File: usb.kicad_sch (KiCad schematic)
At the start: 125 parts, among them J3 USB4105-GF-A, J4 WE_632723300011_alt_symbol, Q1 PJE138K, U10 TUSB1046-DCI, U11 TPD4E05U06QDQARQ1, U12 AP22615, U13 TPD4E05U06QDQARQ1, U14 TPD4E05U06QDQARQ1, U15 TPD4E05U06QDQARQ1, U16 TPD4E05U06QDQARQ1, U5 FT230XQ-R, U6 TPS65988, U7 W25Q80DVUXIE_TR, U8 NCP730BMT330TBG, U9 AP22615

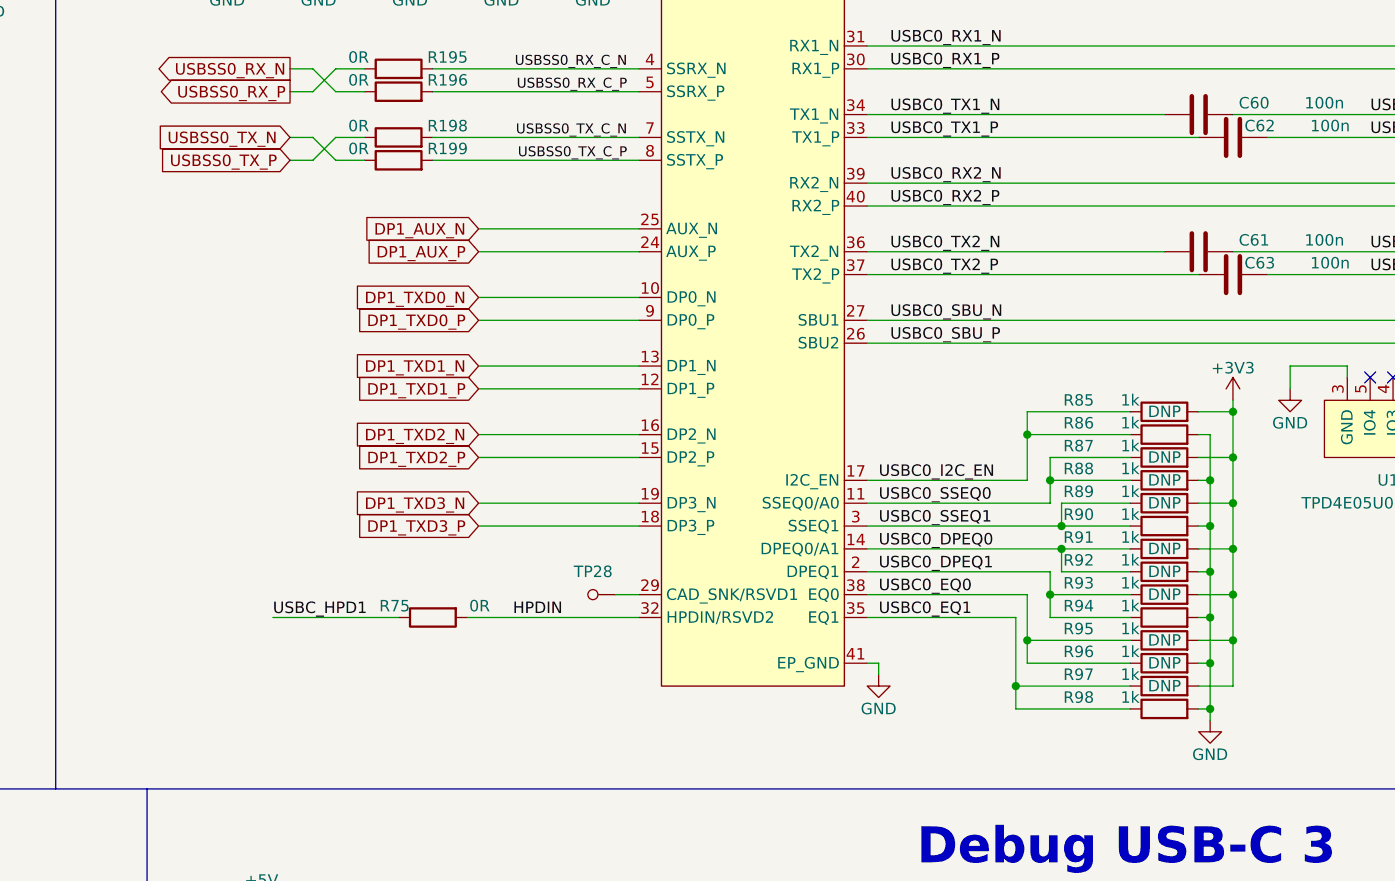
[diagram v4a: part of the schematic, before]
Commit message: Add missing DP AUX pullup/down resistors
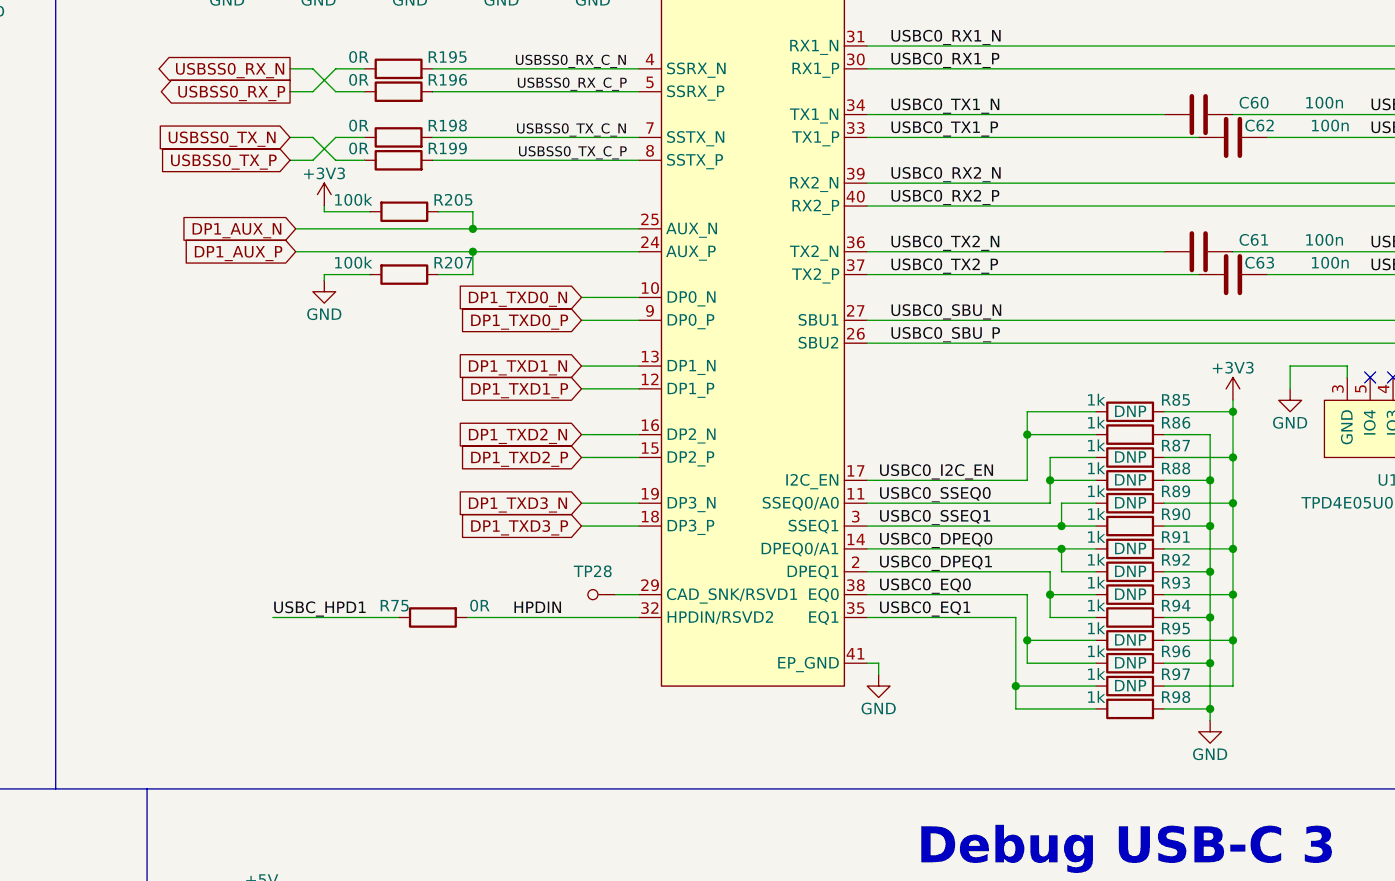
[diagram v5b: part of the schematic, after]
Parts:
- added R205, R207: R_100k_0402, jetson-orin-baseboard-footprints:0402-res, symbol jetson-orin-baseboard:R_100k_0402
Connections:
- net +3V3: now also R205.2
- net DP1_AUX_N: now also R205.1
- net DP1_AUX_P: now also R207.1
- net GND: now also R207.2
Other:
- moved on the sheet: R85, R86, R87, R88, R89, R90, R91, R92, R93, R94, R95, R96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

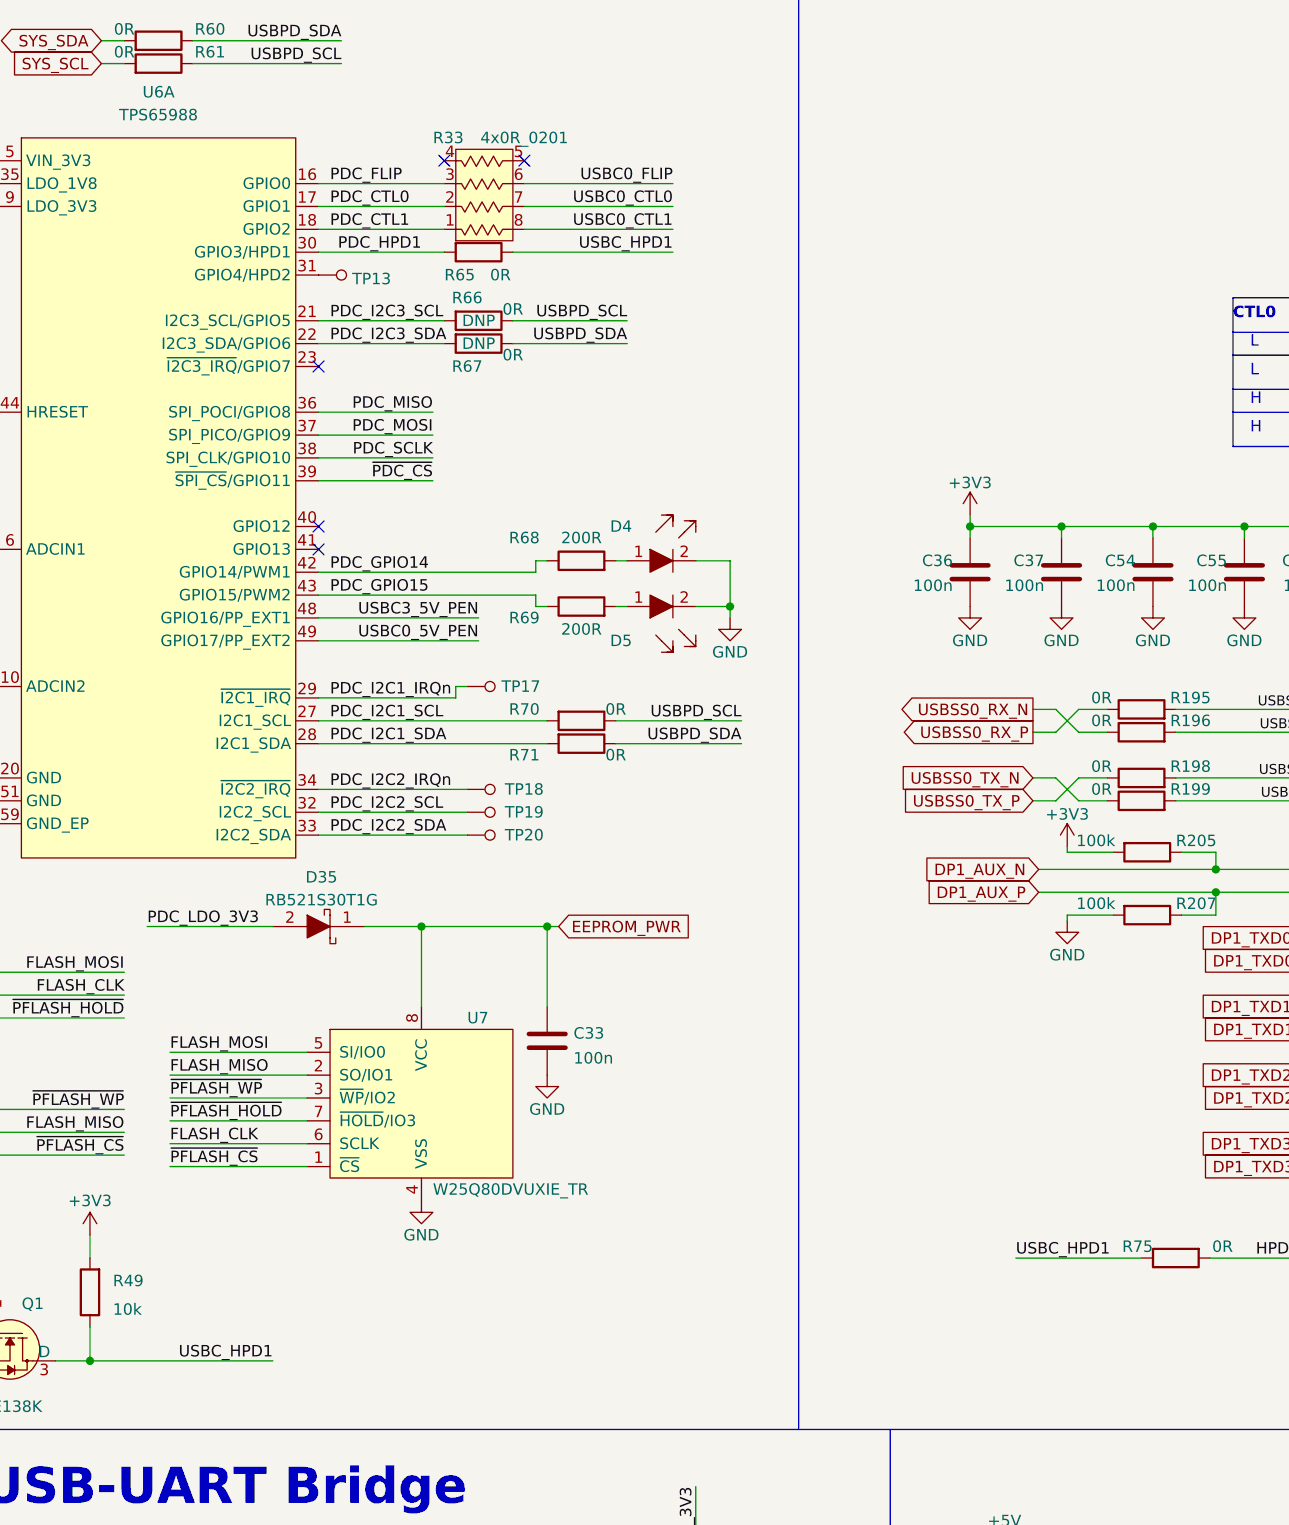
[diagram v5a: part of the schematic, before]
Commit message: Connect USB-C HPD to correct pin
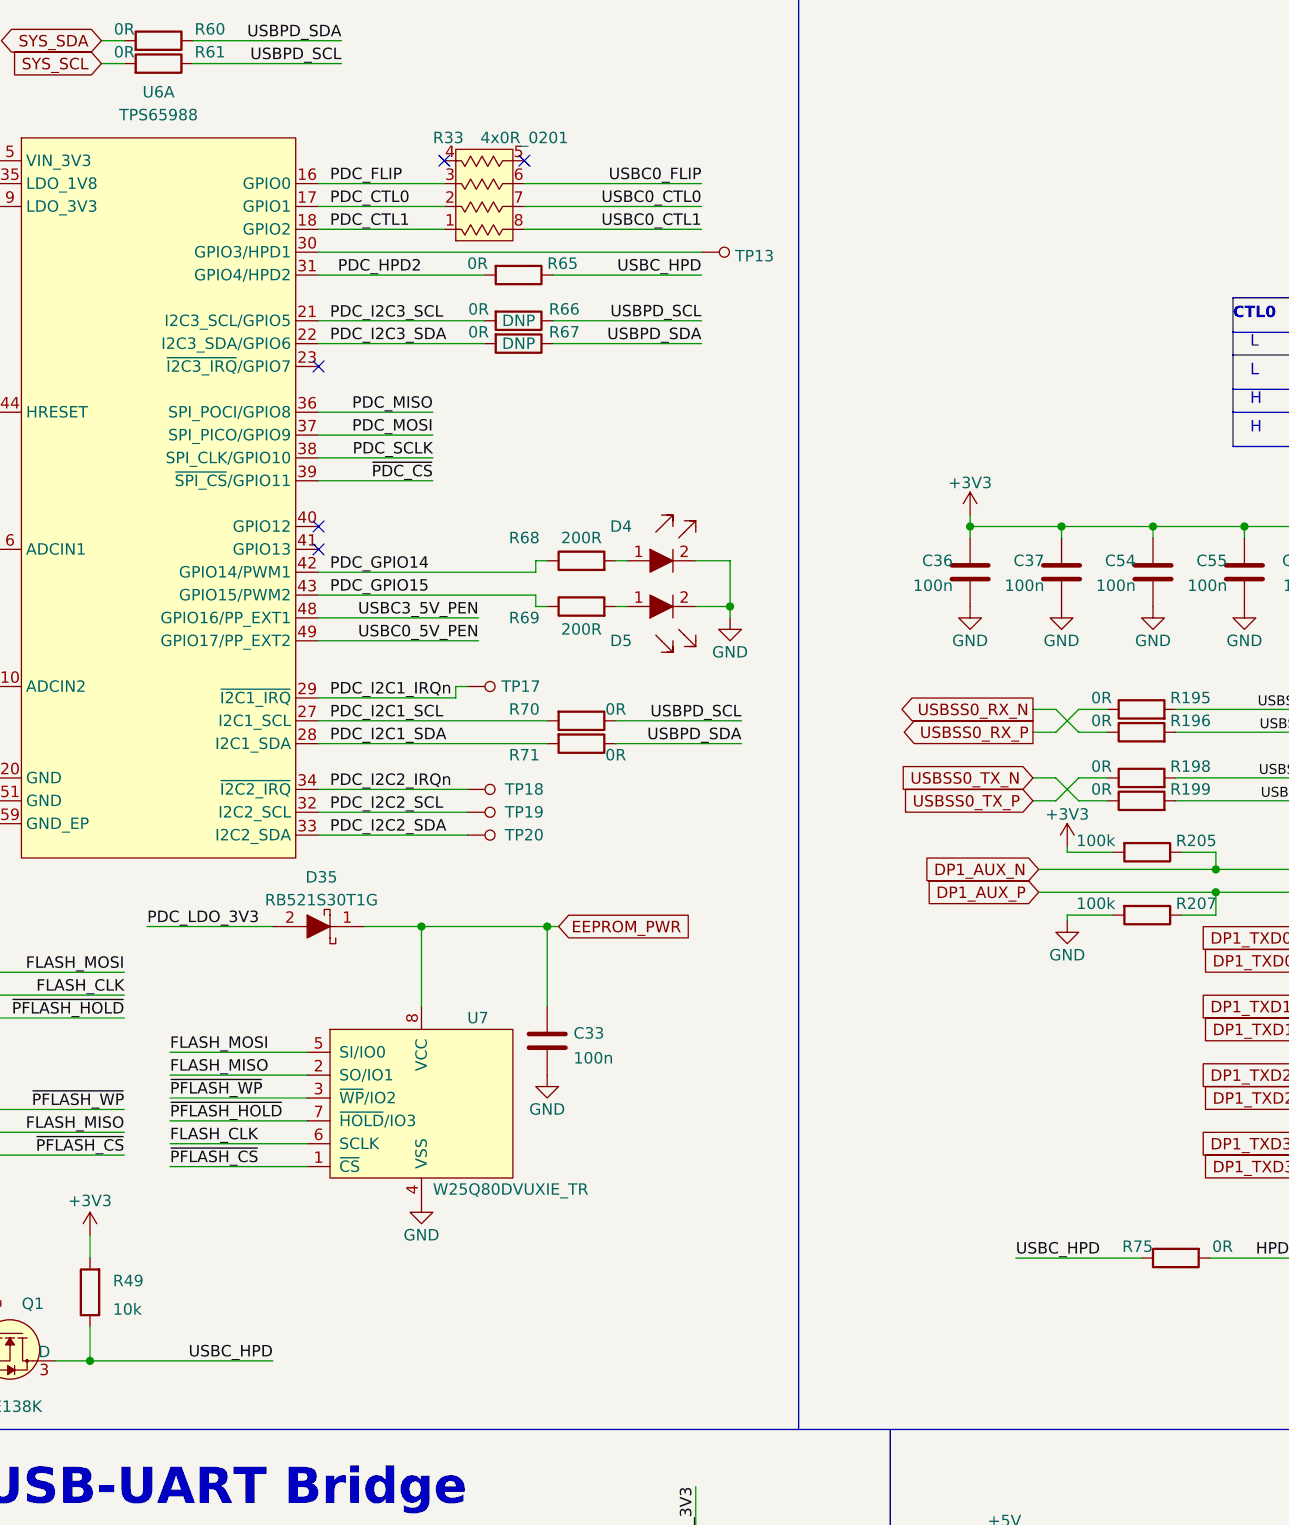
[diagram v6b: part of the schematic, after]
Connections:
- net PDC_I2C3_SCL: no longer R66.2, U6.21 (I2C3_SCL/GPIO5)
- net at TP13.1: now also U6.30 (GPIO3/HPD1); no longer U6.31 (GPIO4/HPD2)
- net PDC_HPD1 renamed PDC_HPD2
- net PDC_HPD2: now also U6.31 (GPIO4/HPD2); no longer U6.30 (GPIO3/HPD1)
- net USBC_HPD1 renamed USBC_HPD
- new net: R66.2, U6.21 (I2C3_SCL/GPIO5)
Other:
- moved on the sheet: R65, R66, R67, TP13

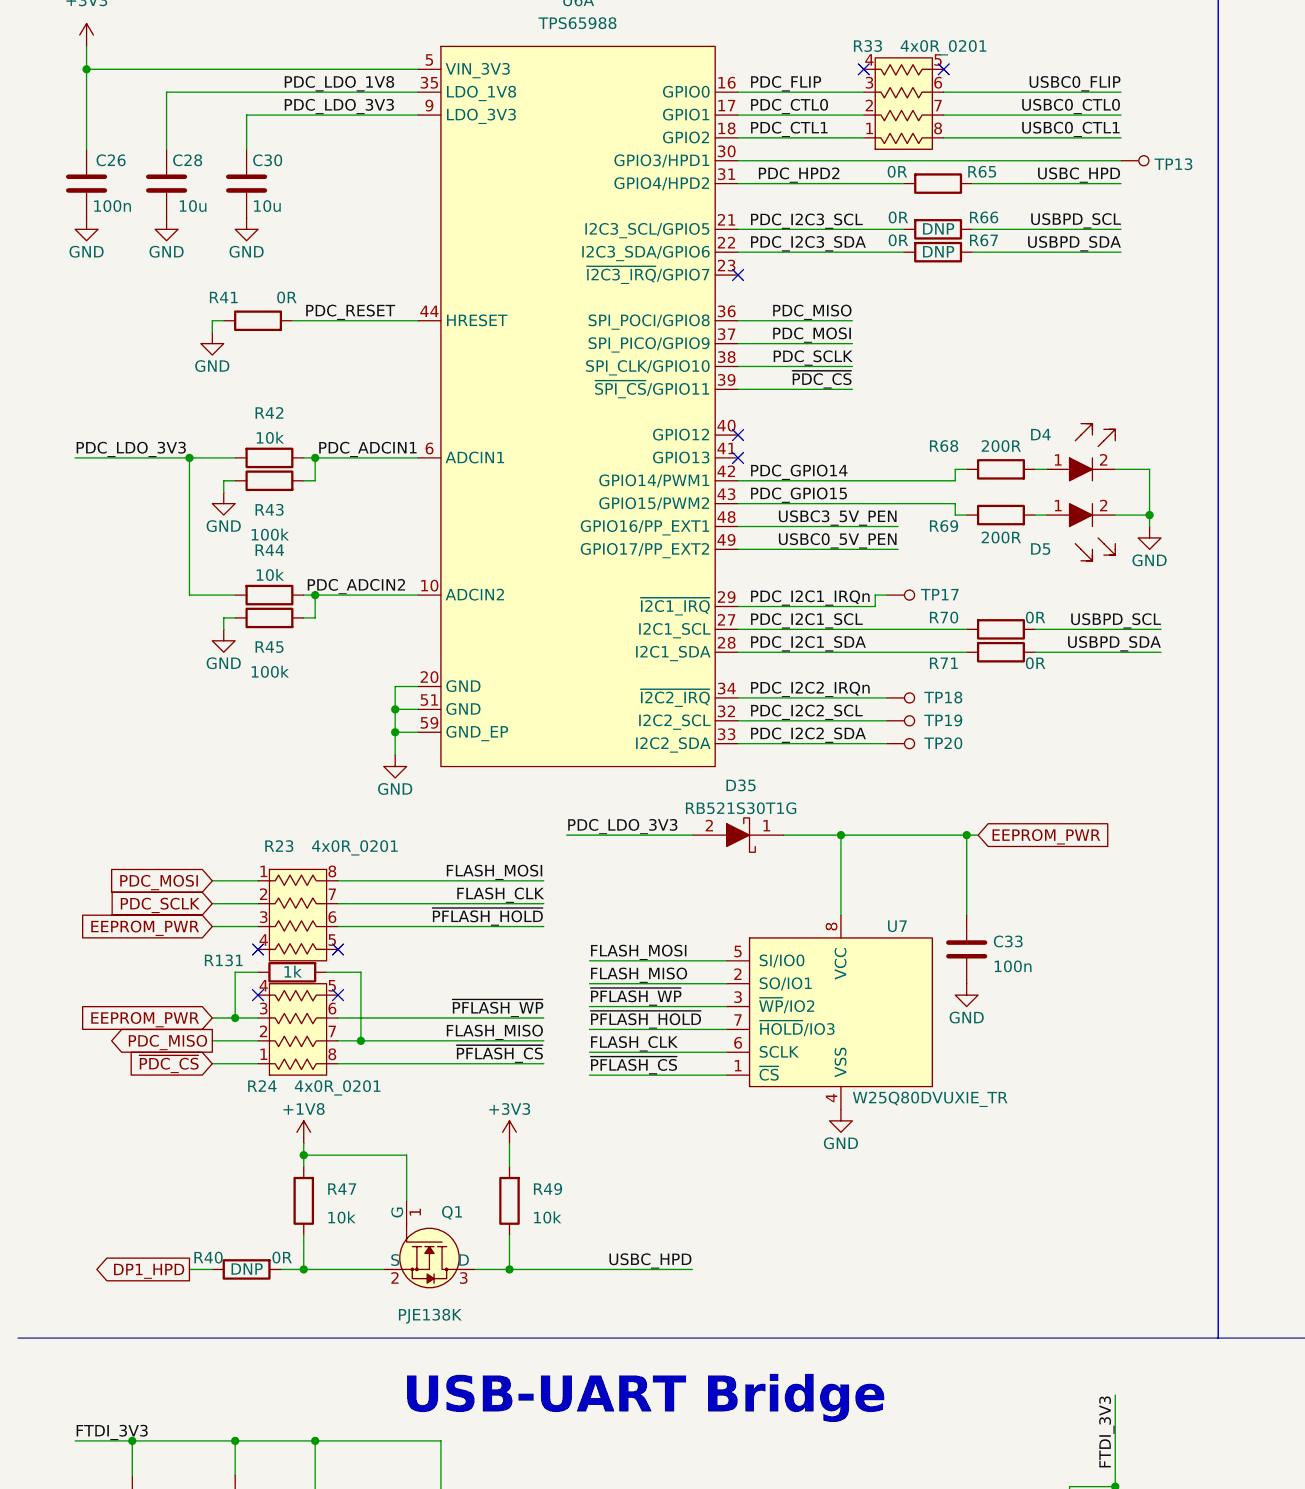
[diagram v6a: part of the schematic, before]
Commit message: Use DP switch in place of selection via mounting option
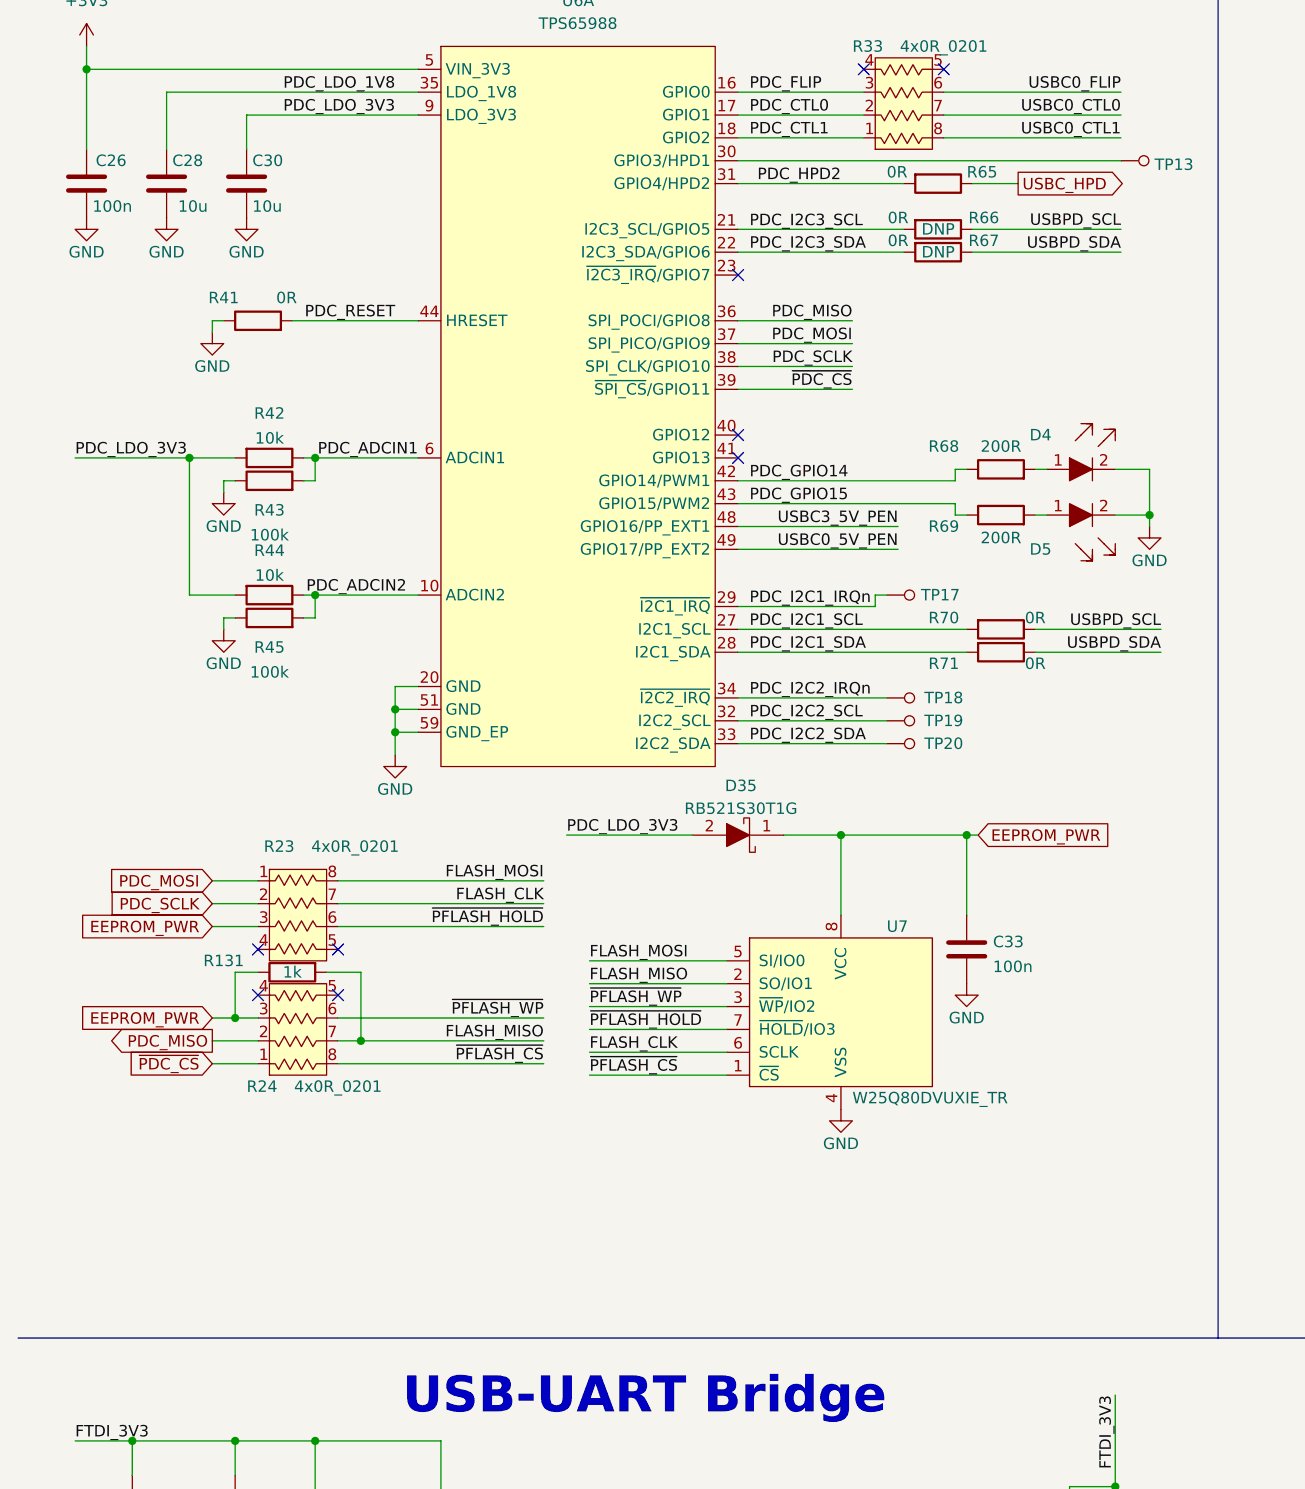
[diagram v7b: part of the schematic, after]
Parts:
- removed Q1: PJE138K, antmicro-footprints:SOT-523, symbol antmicroTransistorsFETsMOSFETsSingle:PJE138K
- removed R40: R_0R_0402, jetson-orin-baseboard-footprints:0402-res, symbol jetson-orin-baseboard:R_0R_0402
- removed R47, R49: R_10k_0402, jetson-orin-baseboard-footprints:0402-res, symbol jetson-orin-baseboard:R_10k_0402
